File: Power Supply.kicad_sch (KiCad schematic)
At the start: 6 parts, among them U2 TPS61023DRLT

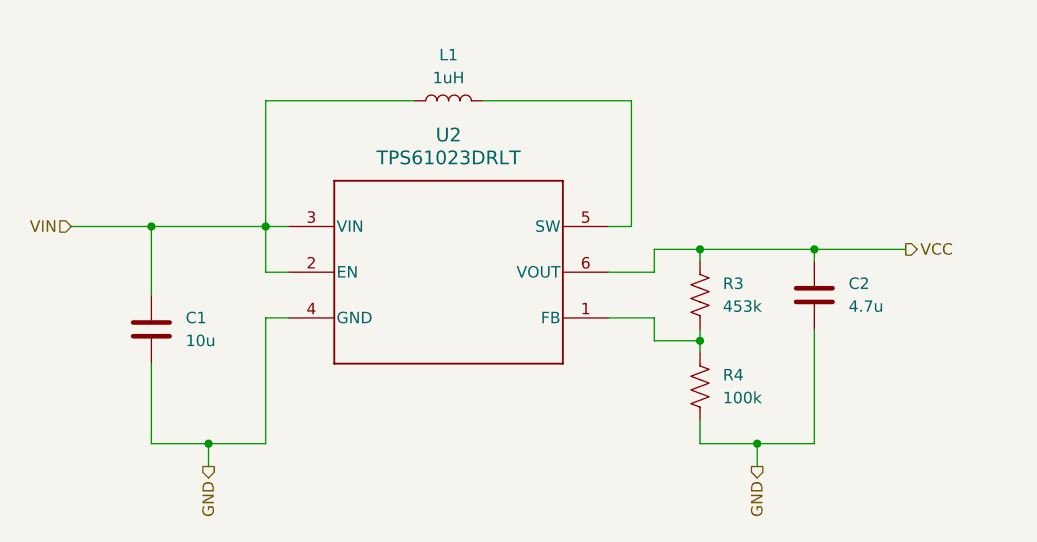
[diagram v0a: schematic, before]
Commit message: add ADC circuit, a few more DNP components, and assigned footprints
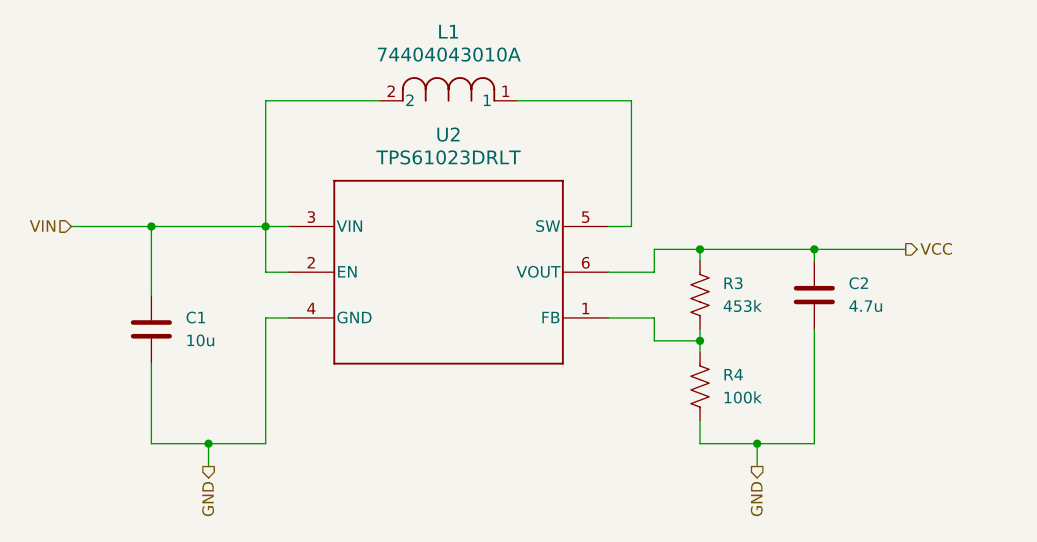
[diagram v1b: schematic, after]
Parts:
- removed L1: 1uH, symbol Device:L
- added L1: 74404043010A, 74404043010A:IND_43010A_WRE, symbol 74404043010A:74404043010A
- C1, C2: footprint (none) -> Capacitor_SMD:C_0603_1608Metric
- R3, R4: footprint (none) -> Resistor_SMD:R_0603_1608Metric
- U2: footprint DRL0006A -> TPS61023DRLT:DRL0006A
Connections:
- net VIN: now also L1.2
- net at U2.5 (SW): now also L1.1
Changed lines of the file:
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@@
   (junction (at 172.72 110.49) (diameter 0) (color 0 0 0 0)
   )
-  (wire (pts (xy 148.59 83.82) (xy 165.1 83.82))
-    (stroke (width 0) (type default))
-  )
   (wire (pts (xy 172.72 121.92) (xy 172.72 119.38))
     (stroke (width 0) (type default))
@@
     (stroke (width 0) (type default))
   )
+  (wire (pts (xy 124.46 83.82) (xy 137.16 83.82))
+    (stroke (width 0) (type default))
+  )
   (wire (pts (xy 165.1 83.82) (xy 165.1 97.79))
     (stroke (width 0) (type default))
@@
     (stroke (width 0) (type default))
   )
+  (wire (pts (xy 152.4 83.82) (xy 165.1 83.82))
+    (stroke (width 0) (type default))
+  )
   (wire (pts (xy 127 107.95) (xy 124.46 107.95))
-    (stroke (width 0) (type default))
-  )
-  (wire (pts (xy 124.46 83.82) (xy 140.97 83.82))
     (stroke (width 0) (type default))
   )
@@
       (effects (font (size 1.27 1.27)) (justify left))
     )
-    (property "Footprint" "" (at 173.736 115.824 90)
+    (property "Footprint" "Resistor_SMD:R_0603_1608Metric" (at 173.736 115.824 90)
       (effects (font (size 1.27 1.27)) hide)
     )
@@
     )
   )
+  (symbol (lib_id "74404043010A:74404043010A") (at 137.16 83.82 0) (unit 1)
+    (in_bom yes) (on_board yes) (dnp no) (fields_autoplaced)
+    (property "Reference" "L1" (at 144.78 76.2 0)
+      (effects (font (size 1.524 1.524)))
+    )
+    (property "Value" "74404043010A" (at 144.78 78.74 0)
+      (effects (font (size 1.524 1.524)))
+    )
+    (property "Footprint" "74404043010A:IND_43010A_WRE" (at 137.16 83.82 0)
+      (effects (font (size 1.27 1.27) italic) hide)
+    )
+    (property "Datasheet" "74404043010A" (at 137.16 83.82 0)
+      (effects (font (size 1.27 1.27) italic) hide)
+    )
+    (pin "1")
+    (pin "2")
+    (instances
+      (project "key-fob-pcb"
+        (path "/b002c3bf-fc58-4993-80f7-7914d3aa1ac9/97ab50b4-0765-4242-8cdd-feb1ed8d7056"
+          (reference "L1") (unit 1)
+        )
+      )
+    )
+  )
   (symbol (lib_id "Device:C") (at 111.76 109.22 0) (unit 1)
     (in_bom yes) (on_board yes) (dnp no) (fields_autoplaced)
@@
       (effects (font (size 1.27 1.27)) (justify left))
     )
-    (property "Footprint" "" (at 112.7252 113.03 0)
+    (property "Footprint" "Capacitor_SMD:C_0603_1608Metric" (at 112.7252 113.03 0)
       (effects (font (size 1.27 1.27)) hide)
     )
@@
       (effects (font (size 1.524 1.524)))
     )
-    (property "Footprint" "DRL0006A" (at 144.78 102.87 0)
+    (property "Footprint" "TPS61023DRLT:DRL0006A" (at 144.78 102.87 0)
       (effects (font (size 1.27 1.27) italic) hide)
     )
@@
       (effects (font (size 1.27 1.27)) (justify left))
     )
-    (property "Footprint" "" (at 173.736 105.664 90)
+    (property "Footprint" "Resistor_SMD:R_0603_1608Metric" (at 173.736 105.664 90)
       (effects (font (size 1.27 1.27)) hide)
     )
@@
     )
   )
-  (symbol (lib_id "Device:L") (at 144.78 83.82 90) (unit 1)
-    (in_bom yes) (on_board yes) (dnp no) (fields_autoplaced)
-    (property "Reference" "L1" (at 144.78 78.74 90)
-      (effects (font (size 1.27 1.27)))
-    )
-    (property "Value" "1uH" (at 144.78 81.28 90)
-      (effects (font (size 1.27 1.27)))
-    )
-    (property "Footprint" "" (at 144.78 83.82 0)
-      (effects (font (size 1.27 1.27)) hide)
-    )
-    (property "Datasheet" "~" (at 144.78 83.82 0)
-      (effects (font (size 1.27 1.27)) hide)
-    )
-    (pin "1")
-    (pin "2")
-    (instances
-      (project "key-fob-pcb"
-        (path "/b002c3bf-fc58-4993-80f7-7914d3aa1ac9/97ab50b4-0765-4242-8cdd-feb1ed8d7056"
-          (reference "L1") (unit 1)
-        )
-      )
-    )
-  )
   (symbol (lib_id "Device:C") (at 185.42 105.41 0) (unit 1)
     (in_bom yes) (on_board yes) (dnp no) (fields_autoplaced)
@@
       (effects (font (size 1.27 1.27)) (justify left))
     )
-    (property "Footprint" "" (at 186.3852 109.22 0)
-      (effects (font (size 1.27 1.27)) hide)
-    )
+    (property "Footprint" "Capacitor_SMD:C_0603_1608Metric" (at 186.3852 109.22 0)
+      (effects (font (size 1.27 1.27)) hide)
+    )

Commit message: create libraries folder for sharing external libs
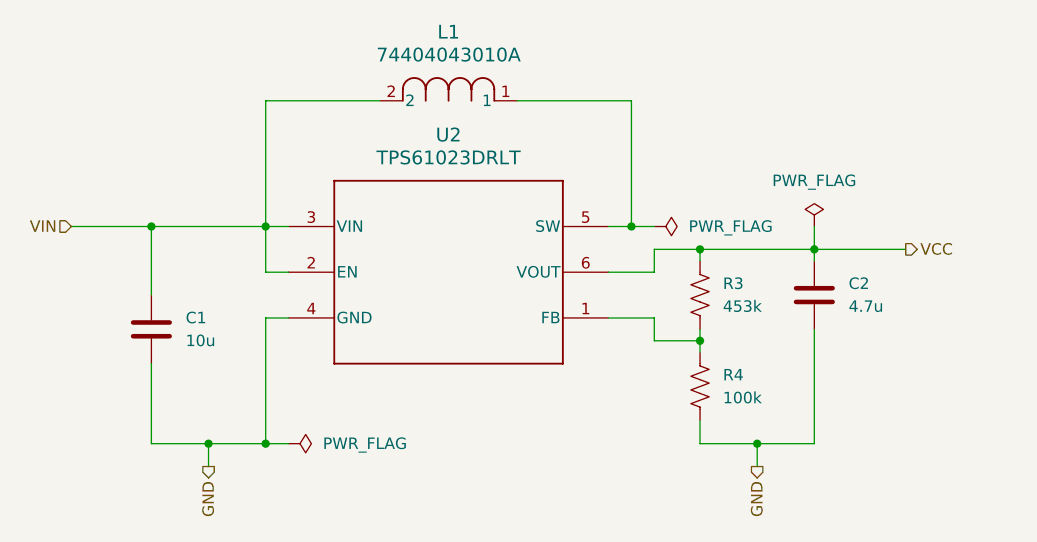
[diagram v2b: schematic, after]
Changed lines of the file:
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@@
   (junction (at 172.72 110.49) (diameter 0) (color 0 0 0 0)
   )
+  (junction (at 165.1 97.79) (diameter 0) (color 0 0 0 0)
+  )
+  (junction (at 124.46 121.92) (diameter 0) (color 0 0 0 0)
+  )
   (wire (pts (xy 172.72 121.92) (xy 172.72 119.38))
     (stroke (width 0) (type default))
@@
     (stroke (width 0) (type default))
   )
+  (wire (pts (xy 124.46 121.92) (xy 127 121.92))
+    (stroke (width 0) (type default))
+  )
   (wire (pts (xy 111.76 121.92) (xy 111.76 113.03))
     (stroke (width 0) (type default))
@@
     (stroke (width 0) (type default))
   )
+  (wire (pts (xy 185.42 97.79) (xy 185.42 100.33))
+    (stroke (width 0) (type default))
+  )
   (wire (pts (xy 124.46 107.95) (xy 124.46 121.92))
     (stroke (width 0) (type default))
@@
   )
   (wire (pts (xy 111.76 105.41) (xy 111.76 97.79))
+    (stroke (width 0) (type default))
+  )
+  (wire (pts (xy 165.1 97.79) (xy 167.64 97.79))
     (stroke (width 0) (type default))
   )
@@
         (path "/b002c3bf-fc58-4993-80f7-7914d3aa1ac9/97ab50b4-0765-4242-8cdd-feb1ed8d7056"
           (reference "R4") (unit 1)
-        )
-      )
-    )
-  )
-  (symbol (lib_id "74404043010A:74404043010A") (at 137.16 83.82 0) (unit 1)
-    (in_bom yes) (on_board yes) (dnp no) (fields_autoplaced)
-    (property "Reference" "L1" (at 144.78 76.2 0)
-      (effects (font (size 1.524 1.524)))
-    )
-    (property "Value" "74404043010A" (at 144.78 78.74 0)
-      (effects (font (size 1.524 1.524)))
-    )
-    (property "Footprint" "74404043010A:IND_43010A_WRE" (at 137.16 83.82 0)
-      (effects (font (size 1.27 1.27) italic) hide)
-    )
-    (property "Datasheet" "74404043010A" (at 137.16 83.82 0)
-      (effects (font (size 1.27 1.27) italic) hide)
-    )
-    (pin "1")
-    (pin "2")
-    (instances
-      (project "key-fob-pcb"
-        (path "/b002c3bf-fc58-4993-80f7-7914d3aa1ac9/97ab50b4-0765-4242-8cdd-feb1ed8d7056"
-          (reference "L1") (unit 1)
         )
       )
@@
     )
   )
+  (symbol (lib_id "74404043010A:74404043010A") (at 137.16 83.82 0) (unit 1)
+    (in_bom yes) (on_board yes) (dnp no) (fields_autoplaced)
+    (property "Reference" "L1" (at 144.78 76.2 0)
+      (effects (font (size 1.524 1.524)))
+    )
+    (property "Value" "74404043010A" (at 144.78 78.74 0)
+      (effects (font (size 1.524 1.524)))
+    )
+    (property "Footprint" "74404043010A:IND_43010A_WRE" (at 137.16 83.82 0)
+      (effects (font (size 1.27 1.27) italic) hide)
+    )
+    (property "Datasheet" "74404043010A" (at 137.16 83.82 0)
+      (effects (font (size 1.27 1.27) italic) hide)
+    )
+    (pin "1")
+    (pin "2")
+    (instances
+      (project "key-fob-pcb"
+        (path "/b002c3bf-fc58-4993-80f7-7914d3aa1ac9/97ab50b4-0765-4242-8cdd-feb1ed8d7056"
+          (reference "L1") (unit 1)
+        )
+      )
+    )
+  )
   (symbol (lib_id "Device:R_US") (at 172.72 105.41 0) (unit 1)
     (in_bom yes) (on_board yes) (dnp no) (fields_autoplaced)
@@
     )
   )
+  (symbol (lib_id "power:PWR_FLAG") (at 185.42 97.79 0) (unit 1)
+    (in_bom yes) (on_board yes) (dnp no) (fields_autoplaced)
+    (property "Reference" "#FLG03" (at 185.42 95.885 0)
+      (effects (font (size 1.27 1.27)) hide)
+    )
+    (property "Value" "PWR_FLAG" (at 185.42 92.71 0)
+      (effects (font (size 1.27 1.27)))
+    )
+    (property "Footprint" "" (at 185.42 97.79 0)
+      (effects (font (size 1.27 1.27)) hide)
+    )
+    (property "Datasheet" "~" (at 185.42 97.79 0)
+      (effects (font (size 1.27 1.27)) hide)
+    )
+    (pin "1")
+    (instances
+      (project "key-fob-pcb"
+        (path "/b002c3bf-fc58-4993-80f7-7914d3aa1ac9/97ab50b4-0765-4242-8cdd-feb1ed8d7056"
+          (reference "#FLG03") (unit 1)
+        )
+      )
+    )
+  )
   (symbol (lib_id "Device:C") (at 185.42 105.41 0) (unit 1)
     (in_bom yes) (on_board yes) (dnp no) (fields_autoplaced)
@@
         )
       )
+    )
+  )
+  (symbol (lib_id "power:PWR_FLAG") (at 127 121.92 270) (unit 1)
+    (in_bom yes) (on_board yes) (dnp no) (fields_autoplaced)
+    (property "Reference" "#FLG05" (at 128.905 121.92 0)
+      (effects (font (size 1.27 1.27)) hide)
+    )
+    (property "Value" "PWR_FLAG" (at 130.81 121.92 90)
+      (effects (font (size 1.27 1.27)) (justify left))
+    )
+    (property "Footprint" "" (at 127 121.92 0)
+      (effects (font (size 1.27 1.27)) hide)
+    )
+    (property "Datasheet" "~" (at 127 121.92 0)
+      (effects (font (size 1.27 1.27)) hide)
+    )
+    (pin "1")
+    (instances
+      (project "key-fob-pcb"
+        (path "/b002c3bf-fc58-4993-80f7-7914d3aa1ac9/97ab50b4-0765-4242-8cdd-feb1ed8d7056"
+          (reference "#FLG05") (unit 1)
+        )
+      )
+    )
+  )
+  (symbol (lib_id "power:PWR_FLAG") (at 167.64 97.79 270) (unit 1)
+    (in_bom yes) (on_board yes) (dnp no) (fields_autoplaced)
+    (property "Reference" "#FLG04" (at 169.545 97.79 0)
+      (effects (font (size 1.27 1.27)) hide)
+    )
+    (property "Value" "PWR_FLAG" (at 171.45 97.79 90)
+      (effects (font (size 1.27 1.27)) (justify left))
+    )
+    (property "Footprint" "" (at 167.64 97.79 0)
+      (effects (font (size 1.27 1.27)) hide)
+    )
+    (property "Datasheet" "~" (at 167.64 97.79 0)
+      (effects (font (size 1.27 1.27)) hide)
+    )
+    (pin "1")
+    (instances
+      (project "key-fob-pcb"
+        (path "/b002c3bf-fc58-4993-80f7-7914d3aa1ac9/97ab50b4-0765-4242-8cdd-feb1ed8d7056"
+          (reference "#FLG04") (unit 1)
+        )
+      )

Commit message: inital layout of components complete
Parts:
- C1, C2: footprint Capacitor_SMD:C_0603_1608Metric -> Capacitor_SMD:C_0402_1005Metric
- R3, R4: footprint Resistor_SMD:R_0603_1608Metric -> Resistor_SMD:R_0402_1005Metric
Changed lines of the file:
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@@
       (effects (font (size 1.27 1.27)) (justify left))
     )
-    (property "Footprint" "Resistor_SMD:R_0603_1608Metric" (at 173.736 115.824 90)
+    (property "Footprint" "Resistor_SMD:R_0402_1005Metric" (at 173.736 115.824 90)
       (effects (font (size 1.27 1.27)) hide)
     )
@@
       (effects (font (size 1.27 1.27)) (justify left))
     )
-    (property "Footprint" "Capacitor_SMD:C_0603_1608Metric" (at 112.7252 113.03 0)
+    (property "Footprint" "Capacitor_SMD:C_0402_1005Metric" (at 112.7252 113.03 0)
       (effects (font (size 1.27 1.27)) hide)
     )
@@
       (effects (font (size 1.27 1.27)) (justify left))
     )
-    (property "Footprint" "Resistor_SMD:R_0603_1608Metric" (at 173.736 105.664 90)
+    (property "Footprint" "Resistor_SMD:R_0402_1005Metric" (at 173.736 105.664 90)
       (effects (font (size 1.27 1.27)) hide)
     )
@@
       (effects (font (size 1.27 1.27)) (justify left))
     )
-    (property "Footprint" "Capacitor_SMD:C_0603_1608Metric" (at 186.3852 109.22 0)
+    (property "Footprint" "Capacitor_SMD:C_0402_1005Metric" (at 186.3852 109.22 0)
       (effects (font (size 1.27 1.27)) hide)
     )

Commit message: generate fab files
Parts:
- C1: MPN (none) -> C3009906
- C2: MPN  (none) -> C2686246
- R3: MPN (none) -> C843903
- R4: MPN (none) -> C844712
- U2: MPN (none) -> C919459
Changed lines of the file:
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@@
+      (effects (font (size 1.27 1.27)) hide)
+    )
+    (property "MPN" "C844712" (at 172.72 115.57 0)
       (effects (font (size 1.27 1.27)) hide)
     )
@@
       (effects (font (size 1.27 1.27)) hide)
     )
+    (property "MPN" "C3009906" (at 111.76 109.22 0)
+      (effects (font (size 1.27 1.27)) hide)
+    )
     (pin "1")
     (pin "2")
@@
     (property "Datasheet" "TPS61023DRLT" (at 144.78 102.87 0)
       (effects (font (size 1.27 1.27) italic) hide)
+    )
+    (property "MPN" "C919459" (at 144.78 102.87 0)
+      (effects (font (size 1.27 1.27)) hide)
     )
     (pin "1")
@@
       (effects (font (size 1.27 1.27)) hide)
     )
+    (property "MPN" "C843903" (at 172.72 105.41 0)
+      (effects (font (size 1.27 1.27)) hide)
+    )
     (pin "1")
     (pin "2")
@@
       (effects (font (size 1.27 1.27)) hide)
     )
+    (property "MPN " "C2686246" (at 185.42 105.41 0)
+      (effects (font (size 1.27 1.27)) hide)
+    )

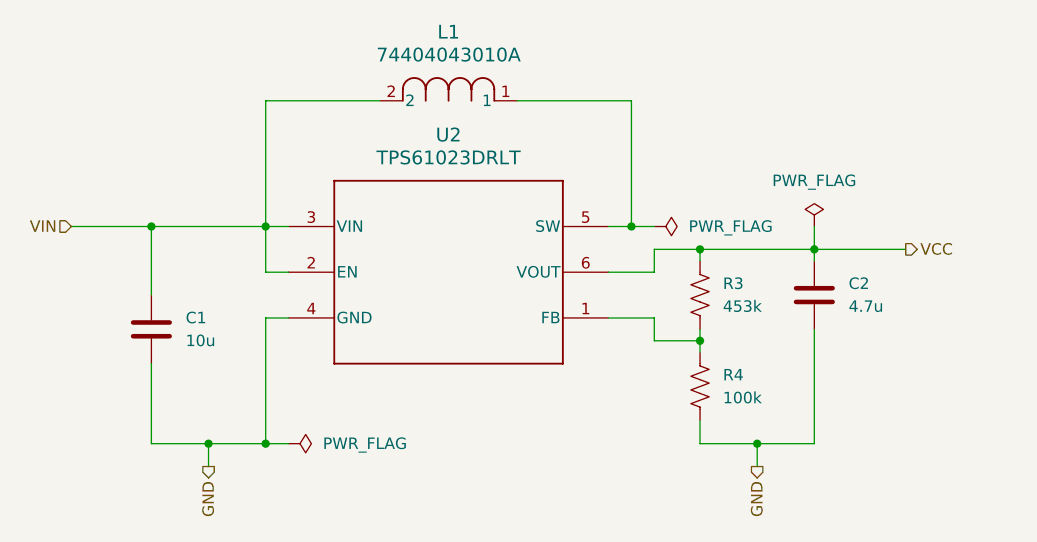
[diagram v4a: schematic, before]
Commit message: replace GND heriarchical labels with GND symbols
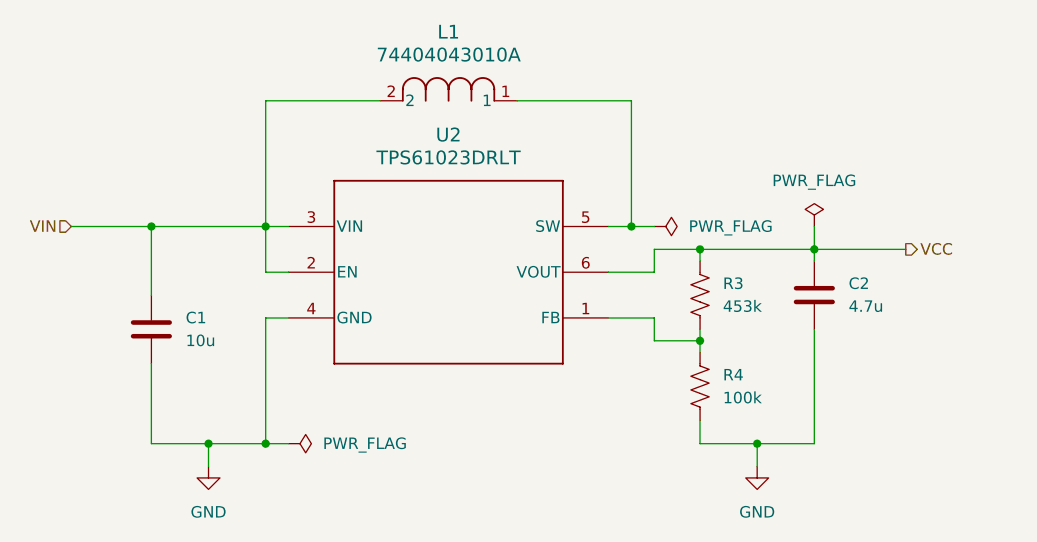
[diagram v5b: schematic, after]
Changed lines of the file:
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@@
     (stroke (width 0) (type default))
-  )
-  (hierarchical_label "GND" (shape output) (at 179.07 124.46 270) (fields_autoplaced)
-    (effects (font (size 1.27 1.27)) (justify right))
   )
   (hierarchical_label "VIN" (shape input) (at 102.87 97.79 180) (fields_autoplaced)
@@
     (effects (font (size 1.27 1.27)) (justify left))
   )
-  (hierarchical_label "GND" (shape output) (at 118.11 124.46 270) (fields_autoplaced)
-    (effects (font (size 1.27 1.27)) (justify right))
-  )
   (symbol (lib_id "Device:R_US") (at 172.72 115.57 0) (unit 1)
     (in_bom yes) (on_board yes) (dnp no) (fields_autoplaced)
@@
         (path "/b002c3bf-fc58-4993-80f7-7914d3aa1ac9/97ab50b4-0765-4242-8cdd-feb1ed8d7056"
           (reference "R4") (unit 1)
+        )
+      )
+    )
+  )
+  (symbol (lib_id "power:GND") (at 118.11 124.46 0) (unit 1)
+    (in_bom yes) (on_board yes) (dnp no) (fields_autoplaced)
+    (property "Reference" "#PWR02" (at 118.11 130.81 0)
+      (effects (font (size 1.27 1.27)) hide)
+    )
+    (property "Value" "GND" (at 118.11 129.54 0)
+      (effects (font (size 1.27 1.27)))
+    )
+    (property "Footprint" "" (at 118.11 124.46 0)
+      (effects (font (size 1.27 1.27)) hide)
+    )
+    (property "Datasheet" "" (at 118.11 124.46 0)
+      (effects (font (size 1.27 1.27)) hide)
+    )
+    (pin "1")
+    (instances
+      (project "key-fob-pcb"
+        (path "/b002c3bf-fc58-4993-80f7-7914d3aa1ac9/97ab50b4-0765-4242-8cdd-feb1ed8d7056"
+          (reference "#PWR02") (unit 1)
         )
       )
@@
         )
       )
+    )
+  )
+  (symbol (lib_id "power:GND") (at 179.07 124.46 0) (unit 1)
+    (in_bom yes) (on_board yes) (dnp no) (fields_autoplaced)
+    (property "Reference" "#PWR03" (at 179.07 130.81 0)
+      (effects (font (size 1.27 1.27)) hide)
+    )
+    (property "Value" "GND" (at 179.07 129.54 0)
+      (effects (font (size 1.27 1.27)))
+    )
+    (property "Footprint" "" (at 179.07 124.46 0)
+      (effects (font (size 1.27 1.27)) hide)
+    )
+    (property "Datasheet" "" (at 179.07 124.46 0)
+      (effects (font (size 1.27 1.27)) hide)
+    )
+    (pin "1")
+    (instances
+      (project "key-fob-pcb"
+        (path "/b002c3bf-fc58-4993-80f7-7914d3aa1ac9/97ab50b4-0765-4242-8cdd-feb1ed8d7056"
+          (reference "#PWR03") (unit 1)
+        )
+      )
